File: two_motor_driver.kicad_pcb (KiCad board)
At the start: 4 copper layers, 101 x 60.3 mm, 49 parts, among them J1 Conn_01x02, J2 ESP PROG, J3 Conn_01x01, J4 Conn_01x01, J5 Conn_01x01, J6 Conn_01x08, M1 Conn_01x03, M2 Conn_01x03, SW1 SW_Push, SW2 SW_SPDT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

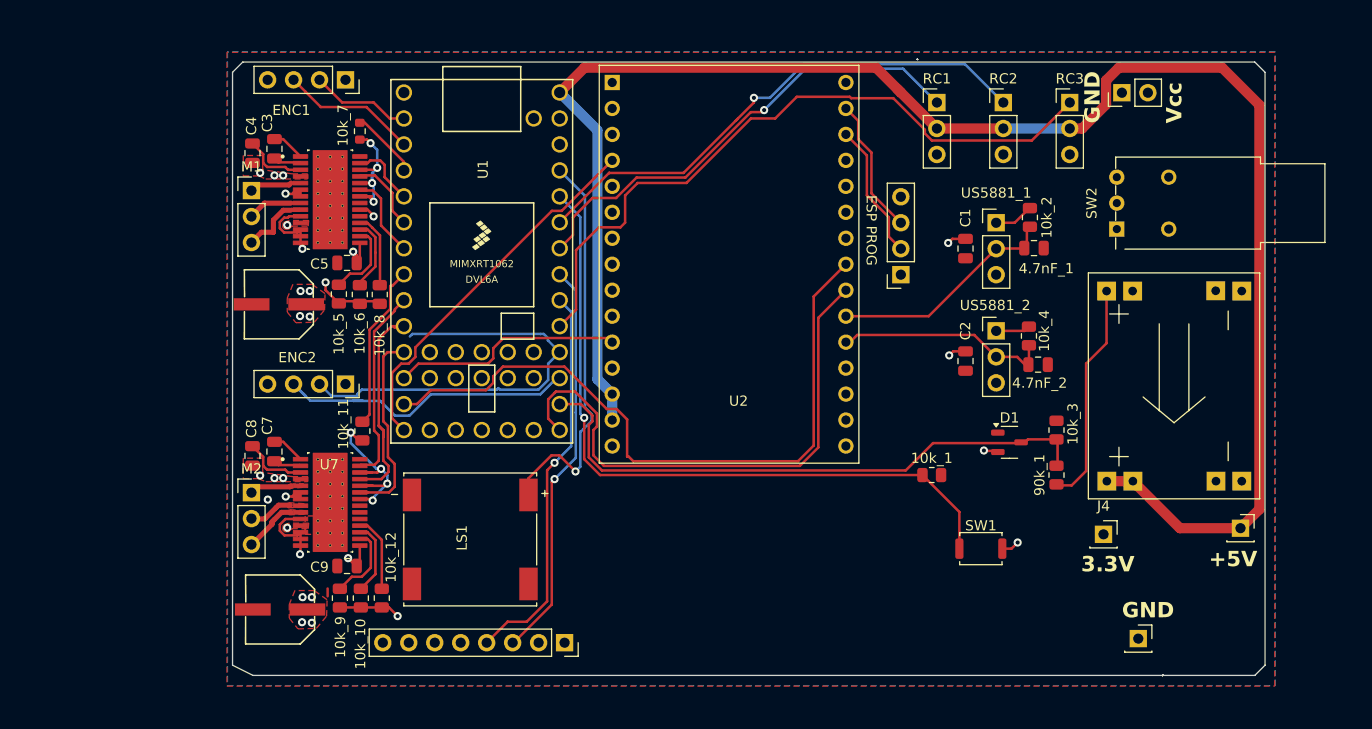
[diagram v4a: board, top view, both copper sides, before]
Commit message: added DRV8313
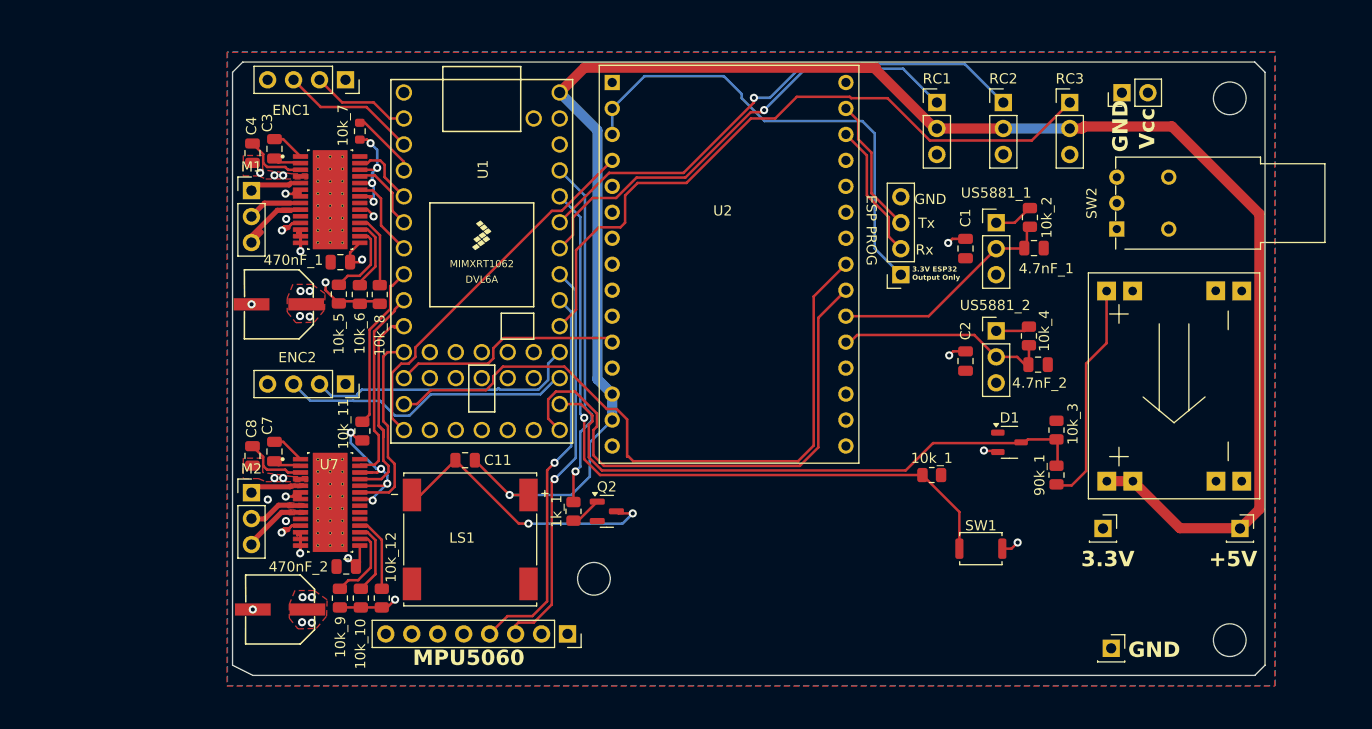
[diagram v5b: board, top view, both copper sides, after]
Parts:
- removed C5, C9: 470nF, Capacitor_SMD:C_0805_2012Metric
- added 1k_1: 10k, Resistor_SMD:R_0805_2012Metric, F.Cu at (146.2, 134.8)
- added 470nF_1: 470nF, Capacitor_SMD:C_0805_2012Metric, F.Cu at (123.4, 110.4)
- added 470nF_2: 470nF, Capacitor_SMD:C_0805_2012Metric, F.Cu at (124.0, 140.2)
- added C11: 100nF, Capacitor_SMD:C_0805_2012Metric, F.Cu at (135.6, 129.8)
- added Q2: my_BC337, Package_TO_SOT_SMD:SOT-23, F.Cu at (149.5, 134.8)
- added REF**: MountingHole_3.2mm_M3, MountingHole:MountingHole_3.2mm_M3, F.Cu at (148.2, 141.4)
- added REF**: MountingHole_3.2mm_M3, MountingHole:MountingHole_3.2mm_M3, F.Cu at (210.4, 147.4)
- added REF**: MountingHole_3.2mm_M3, MountingHole:MountingHole_3.2mm_M3, F.Cu at (210.4, 94.4)
- moved J5 2.82 mm to (198.8, 148.2)
- moved J6 0.91 mm to (145.6, 146.8)
- moved J4 0.58 mm to (198.0, 136.5)
- moved J3 0.06 mm to (211.4, 136.5)
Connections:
- J2 pad 1: +3.3V -> /teensy/+3.3V OUTPUT
- LS1 pad 1: /teensy/SPEAKER -> +5V
- LS1 pad 2: GND -> Net-(Q2-C)
- U2 pad 2: unconnected-(U2-3V3-Pad2) -> /teensy/+3.3V OUTPUT
- U2 pad 3: unconnected-(U2-3V3-Pad2)_1 -> /teensy/+3.3V OUTPUT
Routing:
- net /teensy/+3.3V OUTPUT: track 0.00 -> 47.0 mm
- net Net-(Q2-C): track 0.00 -> 27.7 mm, vias 0 -> 2
- net /teensy/ENC2_A: track 42.5 -> 26.9 mm
- net +5V: track 169.2 -> 179.3 mm, vias 0 -> 1
- net /teensy/SPEAKER: track 39.2 -> 34.5 mm
- net Vcc: track 232.0 -> 236.3 mm, vias 16 -> 15
- net Net-(Q2-B): track 0.00 -> 3.10 mm
- net /teensy/ENC2_B: track 31.9 -> 28.8 mm
- net Net-(M2-Pin_2): track 4.36 -> 6.18 mm
- net Net-(M1-Pin_3): track 8.25 -> 9.90 mm
- net Net-(U7-EN1): track 19.2 -> 17.9 mm
- net +3.3V: track 34.1 -> 33.2 mm
- net FOC2_PWM_C: track 19.9 -> 19.0 mm
- net /teensy/MPU6050_SDA: track 38.5 -> 37.8 mm
- net Net-(M1-Pin_1): track 6.66 -> 6.08 mm
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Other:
- board size 101 x 60.3 mm -> 101 x 60 mm
- board text added: "3.3V ESP32 Output Only"
- board text added: "MPU5060"
- board text added: "Rx"
- board text added: "Tx"

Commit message: jlcpcb order Y34-4852697
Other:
- board text added: "MPU6050"
- board text removed: "MPU5060"
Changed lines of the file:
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@@
 		(tags "Through hole pin header THT 1x03 2.54mm single row")
 		(property "Reference" "M2"
-			(at 0 -2.33 0)
+			(at 2.625 1.555 0)
 			(layer "F.SilkS")
 			(effects
@@
 		(tags "resistor")
 		(property "Reference" "10k_12"
-			(at 3.9875 0.9 90)
+			(at 4.2875 0.05 90)
 			(layer "F.SilkS")
 			(effects
@@
 		(tags "capacitor")
 		(property "Reference" "C3"
-			(at -2.538679 0.7 90)
+			(at -0.438679 -1.6 90)
 			(layer "F.SilkS")
 			(effects
@@
 		(tags "capacitor")
 		(property "Reference" "470nF_1"
-			(at -4.6 -0.2 0)
+			(at 0.15 1.2 0)
 			(layer "F.SilkS")
 			(effects
 				(font
-					(size 1 1)
-					(thickness 0.15)
+					(size 0.5 0.5)
+					(thickness 0.08)
 				)
 			)
@@
 		(tags "capacitor")
 		(property "Reference" "C11"
-			(at -3.2 0 360)
+			(at -3.2 0 0)
 			(layer "F.SilkS")
 			(effects
@@
 		)
 		(property "Value" "100nF"
-			(at 0 1.68 360)
+			(at 0 1.68 0)
 			(layer "F.Fab")
 			(effects
@@
 		)
 		(fp_text user "${REFERENCE}"
-			(at 0 0 360)
+			(at 0 0 0)
 			(layer "F.Fab")
 			(effects
@@
 		(tags "SOT TO_SOT_SMD")
 		(property "Reference" "Q2"
-			(at 0 -2.4 360)
+			(at 2.3625 -1.625 0)
 			(layer "F.SilkS")
 			(effects
@@
 		)
 		(property "Value" "my_BC337"
-			(at 0 2.4 360)
+			(at 0 2.4 0)
 			(layer "F.Fab")
 			(effects
@@
 		)
 		(property "Footprint" "Package_TO_SOT_SMD:SOT-23"
-			(at 0 0 360)
+			(at 0 0 0)
 			(layer "F.Fab")
 			(hide yes)
@@
 		)
 		(property "Datasheet" "https://diotec.com/tl_files/diotec/files/pdf/datasheets/bc337.pdf"
-			(at 0 0 360)
+			(at 0 0 0)
 			(layer "F.Fab")
 			(hide yes)
@@
 		)
 		(property "Description" "0.8A Ic, 45V Vce, NPN Transistor, TO-92"
-			(at 0 0 360)
+			(at 0 0 0)
 			(layer "F.Fab")
 			(hide yes)
@@
 		)
 		(fp_text user "${REFERENCE}"
-			(at 0 0 360)
+			(at 0 0 0)
 			(layer "F.Fab")
 			(effects
@@
 		(tags "Through hole pin header THT 1x03 2.54mm single row")
 		(property "Reference" "M1"
-			(at 0 -2.33 0)
+			(at 2.6 1.45 0)
 			(layer "F.SilkS")
 			(effects
@@
 		(tags "capacitor")
 		(property "Reference" "C7"
-			(at -2.538679 0.7 90)
+			(at -1.125 -1.825 90)
 			(layer "F.SilkS")
 			(effects
@@
 		(tags "Through hole socket strip THT 1x04 2.54mm single row")
 		(property "Reference" "ENC1"
-			(at 2.975 5.3 0)
+			(at 2.311321 4.8 0)
 			(layer "F.SilkS")
 			(effects
@@
 		(tags "capacitor")
 		(property "Reference" "470nF_2"
-			(at -4.675 0.025 0)
+			(at -3.3 -0.175 0)
 			(layer "F.SilkS")
 			(effects
 				(font
-					(size 1 1)
-					(thickness 0.15)
+					(size 0.5 0.5)
+					(thickness 0.08)
 				)
 			)
@@
 	)
 	(gr_text "Vcc"
-		(at 203.2 99.37 90)
+		(at 203.525 99.575 90)
 		(layer "F.SilkS")
 		(effects
@@
 		)
 	)
-	(gr_text "MPU5060"
+	(gr_text "MPU6050\n"
 		(at 130.47 150.01 0)
 		(layer "F.SilkS")
@@
 	)
 	(gr_text "GND"
-		(at 200.58 99.67 90)
+		(at 200.75 100.05 90)
 		(layer "F.SilkS")
 		(effects
